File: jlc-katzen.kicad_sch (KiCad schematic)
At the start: 47 parts, among them J1 USB_C_Receptacle_USB2.0_16P, J2 Conn_01x04, J3 Conn_01x04, J4 Conn_01x02, J5 Conn_ARM_SWD_TagConnect_TC2030, Q1 2N7002, Q2 2N7002, Q3 2N7002, U1 XC6206P332MR, U2 W25Q128JVSIQ, U3 RP2040, U4 IRM-H638T/TR2, Y1 12 MHz 20 pF X322512MSB4SI

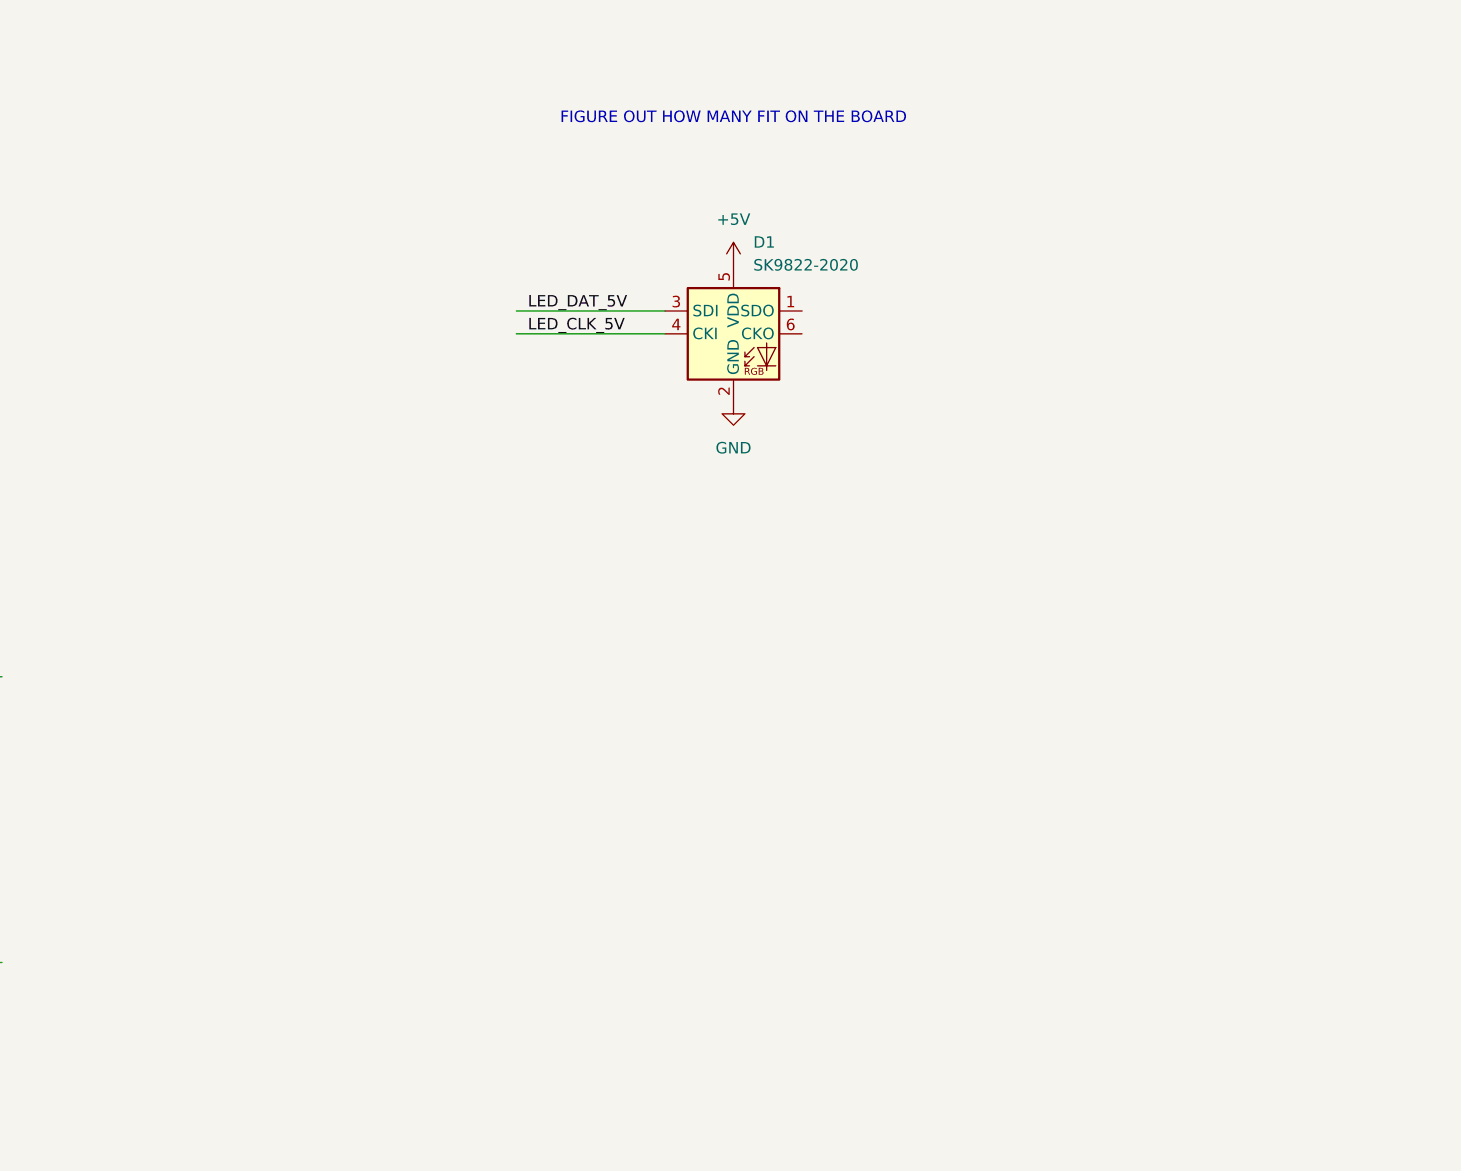
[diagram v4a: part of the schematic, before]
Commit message: hopefully fit this many leds
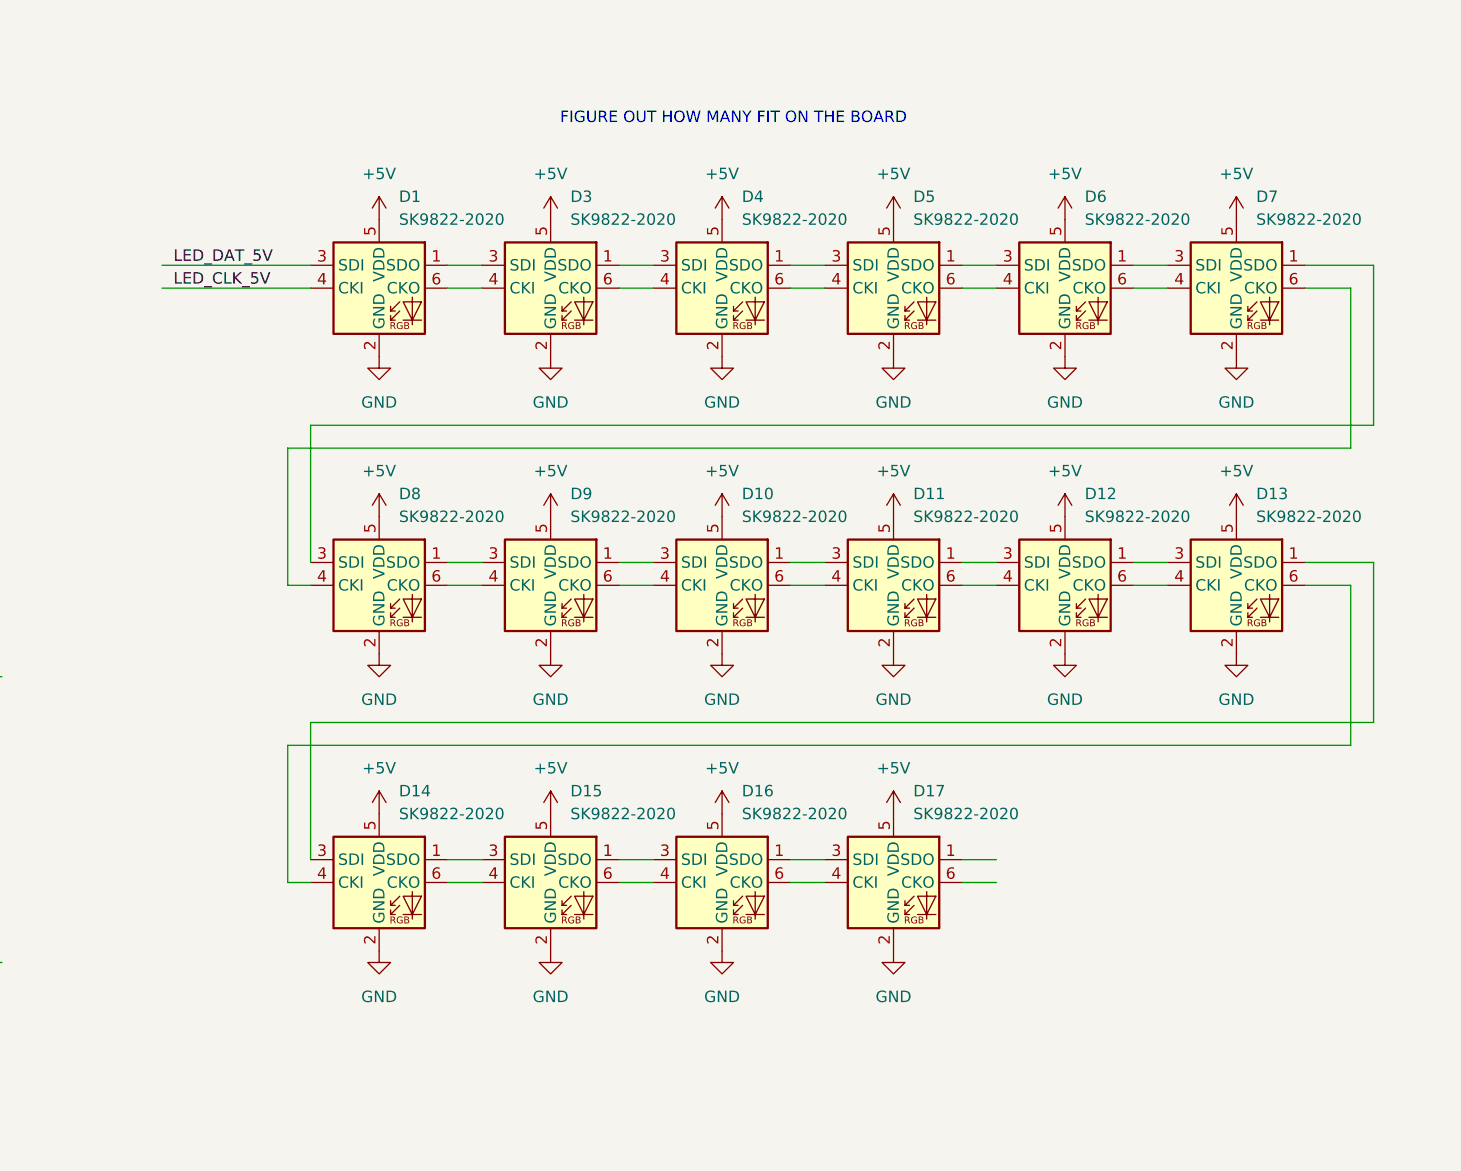
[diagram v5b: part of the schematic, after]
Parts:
- added D10, D11, D12, D13, D14, D15, D16, D17, D3, D4, D5, D6, D7, D8, D9: SK9822-2020, custom_parts:LED-SK9822-2020, symbol custom_parts:SK9822-2020
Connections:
- net +5V: now also D10.5 (VDD), D11.5 (VDD), D12.5 (VDD), D13.5 (VDD), D14.5 (VDD), D15.5 (VDD), D16.5 (VDD), D17.5 (VDD), D3.5 (VDD), D4.5 (VDD), D5.5 (VDD), D6.5 (VDD), D7.5 (VDD), D8.5 (VDD), D9.5 (VDD)
- net GND: now also D10.2 (GND), D11.2 (GND), D12.2 (GND), D13.2 (GND), D14.2 (GND), D15.2 (GND), D16.2 (GND), D17.2 (GND), D3.2 (GND), D4.2 (GND), D5.2 (GND), D6.2 (GND), D7.2 (GND), D8.2 (GND), D9.2 (GND)
- net at D1.1 (SDO): now also D3.3 (SDI)
- net at D1.6 (CKO): now also D3.4 (CKI)
- new net: D7.1 (SDO), D8.3 (SDI)
- new net: D6.1 (SDO), D7.3 (SDI)
- new net: D6.6 (CKO), D7.4 (CKI)
- new net: D7.6 (CKO), D8.4 (CKI)
- new net: D13.1 (SDO), D14.3 (SDI)
- new net: D12.1 (SDO), D13.3 (SDI)
- new net: D12.6 (CKO), D13.4 (CKI)
- new net: D13.6 (CKO), D14.4 (CKI)
- new net: D5.1 (SDO), D6.3 (SDI)
- new net: D5.6 (CKO), D6.4 (CKI)
- new net: D16.1 (SDO), D17.3 (SDI)
- new net: D16.6 (CKO), D17.4 (CKI)
- new net: D3.1 (SDO), D4.3 (SDI)
- new net: D3.6 (CKO), D4.4 (CKI)
- new net: D14.1 (SDO), D15.3 (SDI)
- new net: D14.6 (CKO), D15.4 (CKI)
- new net: D10.1 (SDO), D11.3 (SDI)
- new net: D10.3 (SDI), D9.1 (SDO)
- new net: D10.4 (CKI), D9.6 (CKO)
- new net: D10.6 (CKO), D11.4 (CKI)
- new net: D11.1 (SDO), D12.3 (SDI)
- new net: D11.6 (CKO), D12.4 (CKI)
- new net: D4.1 (SDO), D5.3 (SDI)
- new net: D4.6 (CKO), D5.4 (CKI)
- new net: D8.1 (SDO), D9.3 (SDI)
- new net: D8.6 (CKO), D9.4 (CKI)
- new net: D15.1 (SDO), D16.3 (SDI)
- new net: D15.6 (CKO), D16.4 (CKI)
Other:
- moved on the sheet: D1

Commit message: all nets connected
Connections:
- net IR_RX: now also U3.14 (GPIO11); no longer U3.8 (GPIO6)
- net IR_TX: now also U3.13 (GPIO10); no longer U3.9 (GPIO7)
- net PAIR_IN_RX: now also U3.16 (GPIO13); no longer U3.3 (GPIO1)
- net PAIR_IN_TX: now also U3.15 (GPIO12); no longer U3.2 (GPIO0)
- net PAIR_OUT_RX: now also U3.32 (GPIO21); no longer U3.7 (GPIO5)
- net PAIR_OUT_TX: now also U3.31 (GPIO20); no longer U3.6 (GPIO4)
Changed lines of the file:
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@@
 	(wire
 		(pts
-			(xy 152.4 124.46) (xy 172.72 124.46)
+			(xy 152.4 165.1) (xy 172.72 165.1)
 		)
 		(stroke
@@
 	(wire
 		(pts
-			(xy 152.4 132.08) (xy 172.72 132.08)
+			(xy 152.4 142.24) (xy 172.72 142.24)
 		)
 		(stroke
@@
 	(wire
 		(pts
-			(xy 152.4 129.54) (xy 172.72 129.54)
+			(xy 152.4 139.7) (xy 172.72 139.7)
 		)
 		(stroke
@@
 	(wire
 		(pts
-			(xy 152.4 114.3) (xy 172.72 114.3)
+			(xy 152.4 144.78) (xy 172.72 144.78)
 		)
 		(stroke
@@
 	(wire
 		(pts
-			(xy 152.4 116.84) (xy 172.72 116.84)
-		)
-		(stroke
-			(width 0)
-			(type default)
-		)
-	)
-	(wire
-		(pts
-			(xy 152.4 127) (xy 172.72 127)
+			(xy 152.4 147.32) (xy 172.72 147.32)
+		)
+		(stroke
+			(width 0)
+			(type default)
+		)
+	)
+	(wire
+		(pts
+			(xy 152.4 167.64) (xy 172.72 167.64)
 		)
 		(stroke
@@
 	)
 	(label "PAIR_OUT_RX"
-		(at 160.02 127 0)
+		(at 160.02 167.64 0)
 		(fields_autoplaced yes)
 		(effects
@@
 	)
 	(label "IR_RX"
-		(at 166.37 129.54 0)
+		(at 166.37 142.24 0)
 		(fields_autoplaced yes)
 		(effects
@@
 	)
 	(label "IR_TX"
-		(at 166.37 132.08 0)
+		(at 166.37 139.7 0)
 		(fields_autoplaced yes)
 		(effects
@@
 	)
 	(label "PAIR_IN_TX"
-		(at 161.29 114.3 0)
+		(at 161.29 144.78 0)
 		(fields_autoplaced yes)
 		(effects
@@
 	)
 	(label "PAIR_IN_RX"
-		(at 161.29 116.84 0)
+		(at 161.29 147.32 0)
 		(fields_autoplaced yes)
 		(effects
@@
 	)
 	(label "PAIR_OUT_TX"
-		(at 160.02 124.46 0)
-		(fields_autoplaced yes)
-		(effects
+		(at 160.02 165.1 0)
+		(fields_autoplaced yes)
+		(effects

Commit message: mark unused
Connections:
- no-connect marks 3 -> 25
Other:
- note removed: "TODO OPTIMIZE PINOUT"
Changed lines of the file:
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@@
+	)
+	(no_connect
+		(at 152.4 162.56)
+	)
+	(no_connect
+		(at 152.4 127)
+	)
+	(no_connect
+		(at 152.4 137.16)
+	)
+	(no_connect
+		(at 152.4 132.08)
 	)
 	(no_connect
@@
 	)
 	(no_connect
+		(at 152.4 154.94)
+	)
+	(no_connect
+		(at 152.4 152.4)
+	)
+	(no_connect
+		(at 152.4 177.8)
+	)
+	(no_connect
 		(at 45.72 53.34)
 	)
 	(no_connect
+		(at 351.79 144.78)
+	)
+	(no_connect
+		(at 152.4 124.46)
+	)
+	(no_connect
+		(at 152.4 134.62)
+	)
+	(no_connect
+		(at 351.79 142.24)
+	)
+	(no_connect
+		(at 152.4 172.72)
+	)
+	(no_connect
+		(at 152.4 170.18)
+	)
+	(no_connect
+		(at 152.4 116.84)
+	)
+	(no_connect
 		(at 73.66 233.68)
 	)
+	(no_connect
+		(at 152.4 160.02)
+	)
+	(no_connect
+		(at 152.4 114.3)
+	)
+	(no_connect
+		(at 152.4 175.26)
+	)
+	(no_connect
+		(at 152.4 149.86)
+	)
+	(no_connect
+		(at 152.4 157.48)
+	)
+	(no_connect
+		(at 152.4 190.5)
+	)
+	(no_connect
+		(at 152.4 187.96)
+	)
+	(no_connect
+		(at 152.4 129.54)
+	)
 	(wire
 		(pts
@@
 		)
 	)
-	(text "TODO OPTIMIZE PINOUT"
-		(exclude_from_sim no)
-		(at 165.862 102.616 0)
-		(effects
-			(font
-				(size 1.27 1.27)
-			)
-		)
-	)

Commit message: move ir tx/rx to separate pwm blocks
(even if we use PIO instead)
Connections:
- net IR_RX: now also U3.12 (GPIO9); no longer U3.14 (GPIO11)
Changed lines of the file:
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@@
 	)
 	(no_connect
-		(at 152.4 137.16)
+		(at 152.4 142.24)
 	)
 	(no_connect
@@
 	(wire
 		(pts
-			(xy 152.4 142.24) (xy 172.72 142.24)
+			(xy 152.4 137.16) (xy 172.72 137.16)
 		)
 		(stroke
@@
 	)
 	(label "IR_RX"
-		(at 166.37 142.24 0)
+		(at 166.37 137.16 0)
 		(fields_autoplaced yes)
 		(effects
